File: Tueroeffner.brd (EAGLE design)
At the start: 48.2 x 22.9 mm, 41 parts, among them IC1 NCP1117ST33T3G, IC3 M25PE20, K2 EC2-12TNU, Q1 2N7002CK, Q2 2N7002CK

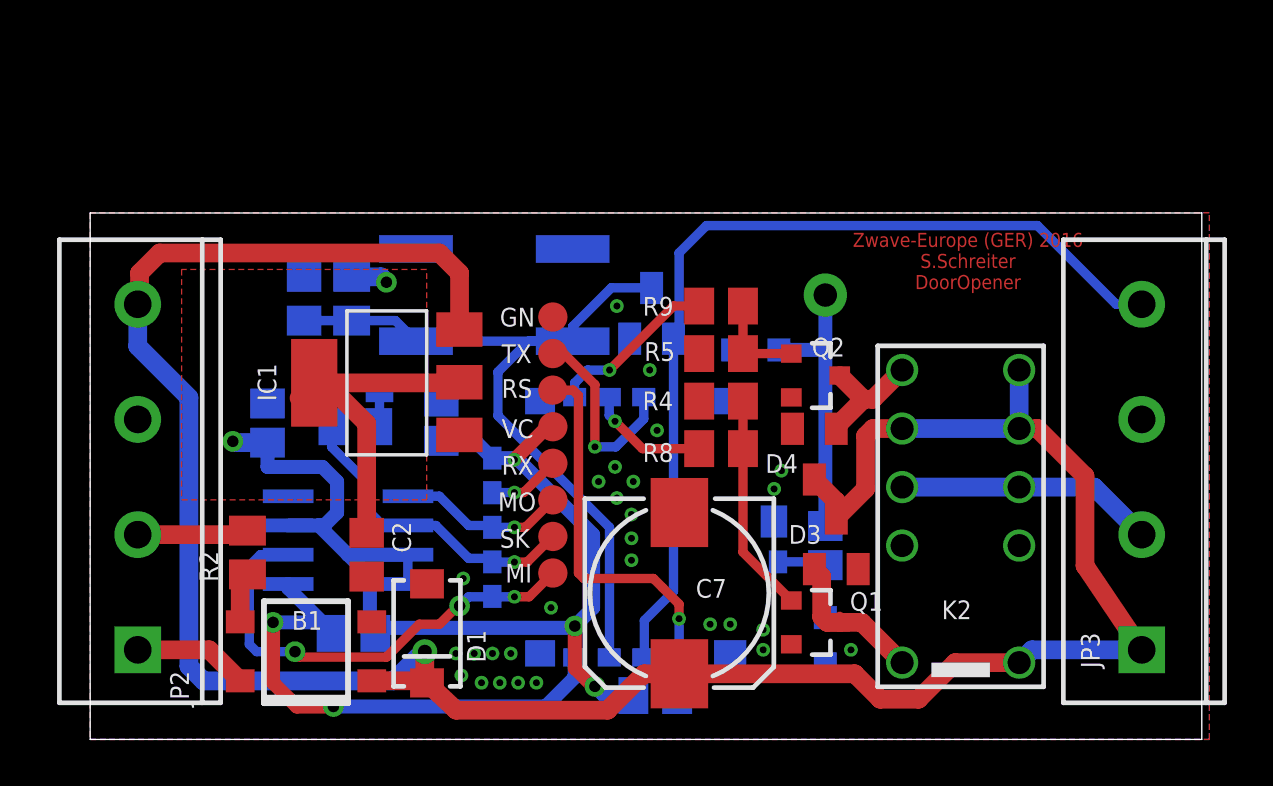
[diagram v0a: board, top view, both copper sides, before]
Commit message: little layout changes
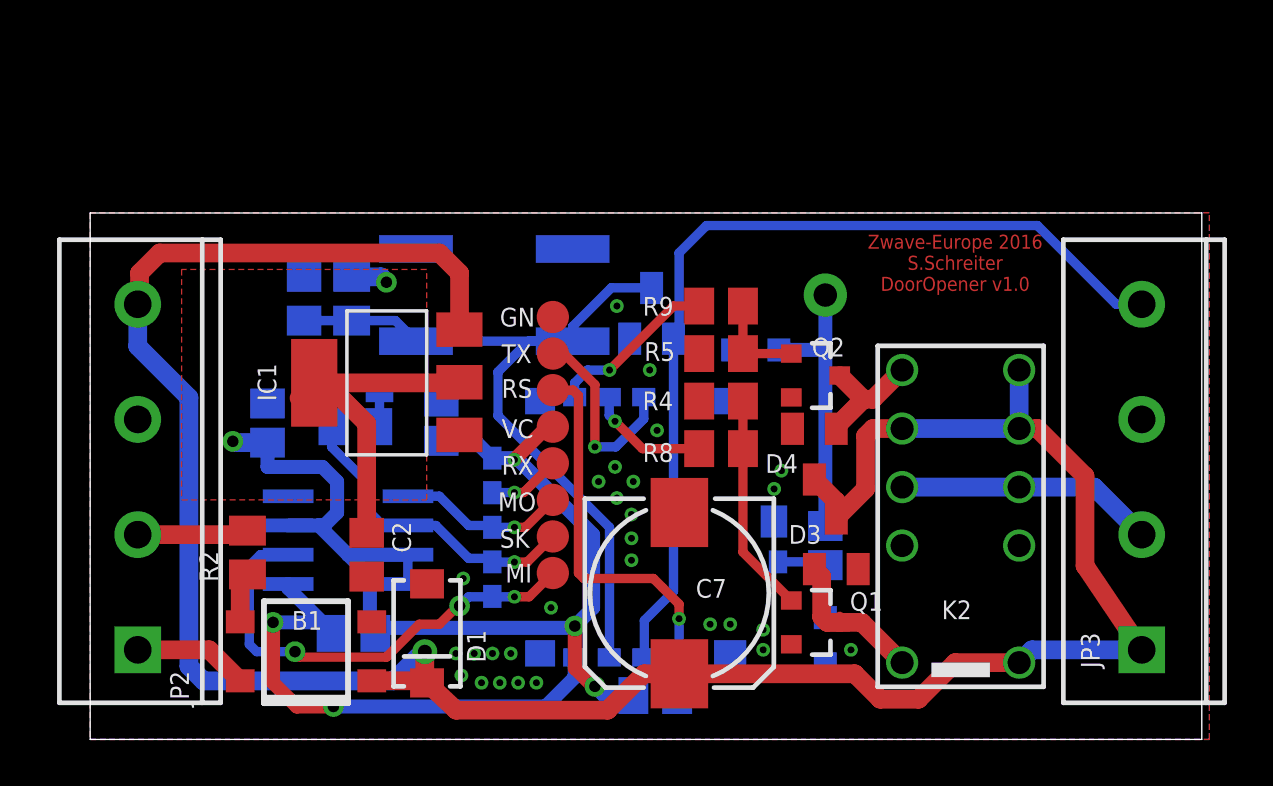
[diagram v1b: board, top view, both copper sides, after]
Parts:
- GN, MI, MO, RS, RX, SK, TX, VC: value TPB1,27 -> TPTP14R; device testpad:B1,27 -> testpad:TP14R
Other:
- board text added: "Zwave-Europe 2016 S.Schreiter DoorOpener v1.0"
- board text removed: "Zwave-Europe (GER) 2016 S.Schreiter DoorOpener"
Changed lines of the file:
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@@
 <layer number="23" name="tOrigins" color="15" fill="1" visible="yes" active="yes"/>
 <layer number="24" name="bOrigins" color="15" fill="1" visible="yes" active="yes"/>
-<layer number="25" name="tNames" color="7" fill="1" visible="yes" active="yes"/>
-<layer number="26" name="bNames" color="7" fill="1" visible="yes" active="yes"/>
+<layer number="25" name="tNames" color="7" fill="1" visible="no" active="yes"/>
+<layer number="26" name="bNames" color="7" fill="1" visible="no" active="yes"/>
 <layer number="27" name="tValues" color="7" fill="1" visible="no" active="yes"/>
 <layer number="28" name="bValues" color="7" fill="1" visible="no" active="yes"/>
@@
 <dimension x1="0" y1="0" x2="0" y2="20" x3="-2" y3="10" textsize="1.778" layer="47"/>
 <dimension x1="0" y1="0" x2="50" y2="0" x3="25" y3="-4" textsize="1.778" layer="47"/>
-<text x="36.5125" y="20.716875" size="0.6096" layer="1" font="vector" ratio="15" rot="R180" align="bottom-center">Zwave-Europe (GER) 2016
+<text x="35.956875" y="20.6375" size="0.6096" layer="1" font="vector" ratio="15" rot="R180" align="bottom-center">Zwave-Europe 2016
 S.Schreiter
-DoorOpener</text>
+DoorOpener v1.0</text>
 <wire x1="46.66" y1="-1.27" x2="46.66" y2="21.59" width="0" layer="20"/>
 </plain>
@@
 <attribute name="VALUE" x="24.526875" y="12.938125" size="1.27" layer="27"/>
 </element>
-<element name="VC" library="testpad" package="B1,27" value="TPB1,27" x="18.494375" y="12.303125" smashed="yes">
+<element name="VC" library="testpad" package="TP14R" value="TPTP14R" x="18.494375" y="12.303125" smashed="yes">
 <attribute name="TP_SIGNAL_NAME" value="" x="17.859375" y="10.398125" size="1" layer="37"/>
 <attribute name="NAME" x="16.271875" y="11.811" size="0.8128" layer="25" ratio="10"/>
 <attribute name="VALUE" x="17.859375" y="11.541125" size="0.0254" layer="27"/>
 </element>
-<element name="RX" library="testpad" package="B1,27" value="TPB1,27" x="18.494375" y="10.715625" smashed="yes">
+<element name="RX" library="testpad" package="TP14R" value="TPTP14R" x="18.494375" y="10.715625" smashed="yes">
 <attribute name="TP_SIGNAL_NAME" value="" x="17.859375" y="8.810625" size="1" layer="37"/>
 <attribute name="NAME" x="16.271875" y="10.2235" size="0.8128" layer="25" ratio="10"/>
 <attribute name="VALUE" x="17.859375" y="9.953625" size="0.0254" layer="27"/>
 </element>
-<element name="TX" library="testpad" package="B1,27" value="TPB1,27" x="18.494375" y="15.478125" smashed="yes">
+<element name="TX" library="testpad" package="TP14R" value="TPTP14R" x="18.494375" y="15.478125" smashed="yes">
 <attribute name="TP_SIGNAL_NAME" value="" x="17.859375" y="13.573125" size="1" layer="37"/>
 <attribute name="NAME" x="16.271875" y="15.065375" size="0.8128" layer="25" ratio="10"/>
 <attribute name="VALUE" x="17.859375" y="14.716125" size="0.0254" layer="27"/>
 </element>
-<element name="GN" library="testpad" package="B1,27" value="TPB1,27" x="18.494375" y="17.065625" smashed="yes">
+<element name="GN" library="testpad" package="TP14R" value="TPTP14R" x="18.494375" y="17.065625" smashed="yes">
 <attribute name="TP_SIGNAL_NAME" value="" x="17.859375" y="15.160625" size="1" layer="37"/>
 <attribute name="NAME" x="16.1925" y="16.652875" size="0.8128" layer="25" ratio="10"/>
 <attribute name="VALUE" x="17.859375" y="16.303625" size="0.0254" layer="27"/>
 </element>
-<element name="MO" library="testpad" package="B1,27" value="TPB1,27" x="18.494375" y="9.128125" smashed="yes">
+<element name="MO" library="testpad" package="TP14R" value="TPTP14R" x="18.494375" y="9.128125" smashed="yes">
 <attribute name="TP_SIGNAL_NAME" value="" x="17.859375" y="7.223125" size="1" layer="37"/>
 <attribute name="NAME" x="16.113125" y="8.636" size="0.8128" layer="25" ratio="10"/>
 <attribute name="VALUE" x="17.859375" y="8.366125" size="0.0254" layer="27"/>
 </element>
-<element name="MI" library="testpad" package="B1,27" value="TPB1,27" x="18.494375" y="5.953125" smashed="yes">
+<element name="MI" library="testpad" package="TP14R" value="TPTP14R" x="18.494375" y="5.953125" smashed="yes">
 <attribute name="TP_SIGNAL_NAME" value="" x="17.859375" y="4.048125" size="1" layer="37"/>
 <attribute name="NAME" x="16.430625" y="5.540375" size="0.8128" layer="25" ratio="10"/>
 <attribute name="VALUE" x="17.859375" y="5.191125" size="0.0254" layer="27"/>
 </element>
-<element name="RS" library="testpad" package="B1,27" value="TPB1,27" x="18.494375" y="13.890625" smashed="yes">
+<element name="RS" library="testpad" package="TP14R" value="TPTP14R" x="18.494375" y="13.890625" smashed="yes">
 <attribute name="TP_SIGNAL_NAME" value="" x="17.859375" y="11.985625" size="1" layer="37"/>
 <attribute name="NAME" x="16.271875" y="13.55725" size="0.8128" layer="25" ratio="10"/>
 <attribute name="VALUE" x="17.859375" y="13.128625" size="0.0254" layer="27"/>
 </element>
-<element name="SK" library="testpad" package="B1,27" value="TPB1,27" x="18.494375" y="7.540625" smashed="yes">
+<element name="SK" library="testpad" package="TP14R" value="TPTP14R" x="18.494375" y="7.540625" smashed="yes">
 <attribute name="TP_SIGNAL_NAME" value="" x="17.859375" y="5.635625" size="1" layer="37"/>
 <attribute name="NAME" x="16.1925" y="7.0485" size="0.8128" layer="25" ratio="10"/>

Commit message: Final RC
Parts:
- added C1: 10µF, eagle-ltspice:C2012
- C6: value 10µF -> 100nF
- IC1: value NCP1117ST33T3G -> NCV4264-2ST33T3G
- LED4: value (none) -> RED
- moved LED4 6.15 mm to (5.16, 17.9), turned to 0 degrees
- moved C2 4.59 mm to (14.4, 9.05)
- moved IC1 1.91 mm to (11.4, 16.1), turned to 270 degrees
- moved C6 1.19 mm to (7.30, 12.5)
- moved R32 0.60 mm to (9.37, 12.5), turned to 90 degrees
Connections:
- net DC_5-12V: now also IC1.1; no longer IC1.3
- net GND: now also C1.2, IC1.2, IC1.4; no longer IC1.1
- net VCC-3.3V: now also C1.1, IC1.3; no longer IC1.2, IC1.4
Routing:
- net DC_5-12V: track 111.0 -> 100.9 mm
- net N$28: track 1.71 -> 5.76 mm
- net VCC-3.3V: track 64.5 -> 66.9 mm
- net BUTTON: track 35.0 -> 33.1 mm
- net RESET: track 17.8 -> 16.1 mm
- net SCK: track 13.7 -> 12.8 mm
- net INT1: track 40.2 -> 39.5 mm
- removed copper zone on layer 1, net VCC-3.3V

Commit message: Add voltage divider
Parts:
- added R6: 180k, resistor:M2012
- added R7: 20k, resistor:M2012
- added SJ1: SOLDERJUMPERTRACE, SparkFun:SJ_2S-TRACE
- moved C2 4.21 mm to (10.8, 11.3), turned to 180 degrees
- moved D1 0.24 mm to (13.0, 3.10)
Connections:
- new net N$2: R6.2, R7.1, SJ1.1
- net DC_5-12V: now also R6.1
- net GND: now also R7.2
- net RXD: now also SJ1.2
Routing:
- net DC_5-12V: track 100.9 -> 113.5 mm
- net N$2: track 0.00 -> 4.73 mm
- net RXD: track 3.16 -> 6.84 mm
- net VCC-3.3V: track 66.9 -> 64.1 mm
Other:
- board text added: "Zwave-Europe 2016 S.Schreiter DoorOpener v1.1"
- board text removed: "Zwave-Europe 2016 S.Schreiter DoorOpener v1.0"

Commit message: BOM
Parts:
- C1, C3: value 10µF -> 100nF
- C5: value 0.1µF -> 100nF
- D1: value SMAJ20A -> SMAJ24A
- IC1: value NCV4264-2ST33T3G -> IFX25001MEV33HTSA1
- R32: value 82 -> 330
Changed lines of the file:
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@@
 <attribute name="VALUE" x="12.064375" y="13.795625" size="1.27" layer="27" rot="R180"/>
 </element>
-<element name="C3" library="eagle-ltspice" package="C2012" value="10µF" x="13.6525" y="12.54125" smashed="yes" rot="MR90">
+<element name="C3" library="eagle-ltspice" package="C2012" value="100nF" x="13.6525" y="12.54125" smashed="yes" rot="MR90">
 <attribute name="SPICEMODEL" value="NONE" x="13.6525" y="12.54125" size="1.778" layer="28" rot="MR90" display="off"/>
 <attribute name="SPICEPREFIX" value="C" x="13.6525" y="12.54125" size="1.778" layer="28" rot="MR90" display="off"/>
@@
 <attribute name="VALUE" x="32.86125" y="8.41375" size="1.27" layer="28" rot="MR270"/>
 </element>
-<element name="C5" library="rcl" package="C0805" value="0.1µF" x="7.699375" y="17.859375" smashed="yes" rot="MR90">
+<element name="C5" library="rcl" package="C0805" value="100nF" x="7.699375" y="17.859375" smashed="yes" rot="MR90">
 <attribute name="NAME" x="8.255" y="20.16125" size="0.8128" layer="26" rot="MR0"/>
 <attribute name="VALUE" x="5.159375" y="16.589375" size="1.27" layer="28" rot="MR90"/>
@@
 <attribute name="VALUE" x="9.8425" y="13.81125" size="1.27" layer="28" rot="MR270"/>
 </element>
-<element name="D1" library="SparkFun-DiscreteSemi" package="SMA-DIODE" value="SMAJ20A" x="13.033125" y="3.09625" smashed="yes" rot="R270">
+<element name="D1" library="SparkFun-DiscreteSemi" package="SMA-DIODE" value="SMAJ24A" x="13.033125" y="3.09625" smashed="yes" rot="R270">
 <attribute name="NAME" x="14.7635" y="3.239125" size="0.8128" layer="25" rot="R270"/>
 <attribute name="VALUE" x="14.684125" y="2.84225" size="0.4064" layer="27" rot="R270"/>
@@
 <attribute name="VALUE" x="24.685625" y="14.049375" size="1.27" layer="28" rot="MR0"/>
 </element>
-<element name="IC1" library="burr-brown" package="SOT223" value="NCV4264-2ST33T3G" x="11.414375" y="16.11375" smashed="yes" rot="R270">
+<element name="IC1" library="burr-brown" package="SOT223" value="IFX25001MEV33HTSA1" x="11.414375" y="16.11375" smashed="yes" rot="R270">
 <attribute name="MPN" value="REG1118-2.85/2K5G4" x="11.414375" y="16.11375" size="1.778" layer="27" rot="R270" display="off"/>
 <attribute name="OC_NEWARK" value="14M2185" x="11.414375" y="16.11375" size="1.778" layer="27" rot="R270" display="off"/>
@@
 <attribute name="VALUE" x="8.5725" y="5.87375" size="1.27" layer="28" rot="MR180"/>
 </element>
-<element name="R32" library="resistor" package="M2012" value="82" x="9.36625" y="12.54125" smashed="yes" rot="MR90">
+<element name="R32" library="resistor" package="M2012" value="330" x="9.36625" y="12.54125" smashed="yes" rot="MR90">
 <attribute name="NAME" x="10.239375" y="14.366875" size="0.8128" layer="26" rot="MR0"/>
 <attribute name="VALUE" x="6.82625" y="11.27125" size="1.27" layer="28" rot="MR90"/>
@@
 <attribute name="VALUE" x="17.859375" y="6.778625" size="0.0254" layer="27"/>
 </element>
-<element name="C1" library="eagle-ltspice" package="C2012" value="10µF" x="11.43" y="12.54125" smashed="yes" rot="MR90">
+<element name="C1" library="eagle-ltspice" package="C2012" value="100nF" x="11.43" y="12.54125" smashed="yes" rot="MR90">
 <attribute name="SPICEMODEL" value="NONE" x="11.43" y="12.54125" size="1.778" layer="28" rot="MR90" display="off"/>
 <attribute name="SPICEPREFIX" value="C" x="11.43" y="12.54125" size="1.778" layer="28" rot="MR90" display="off"/>

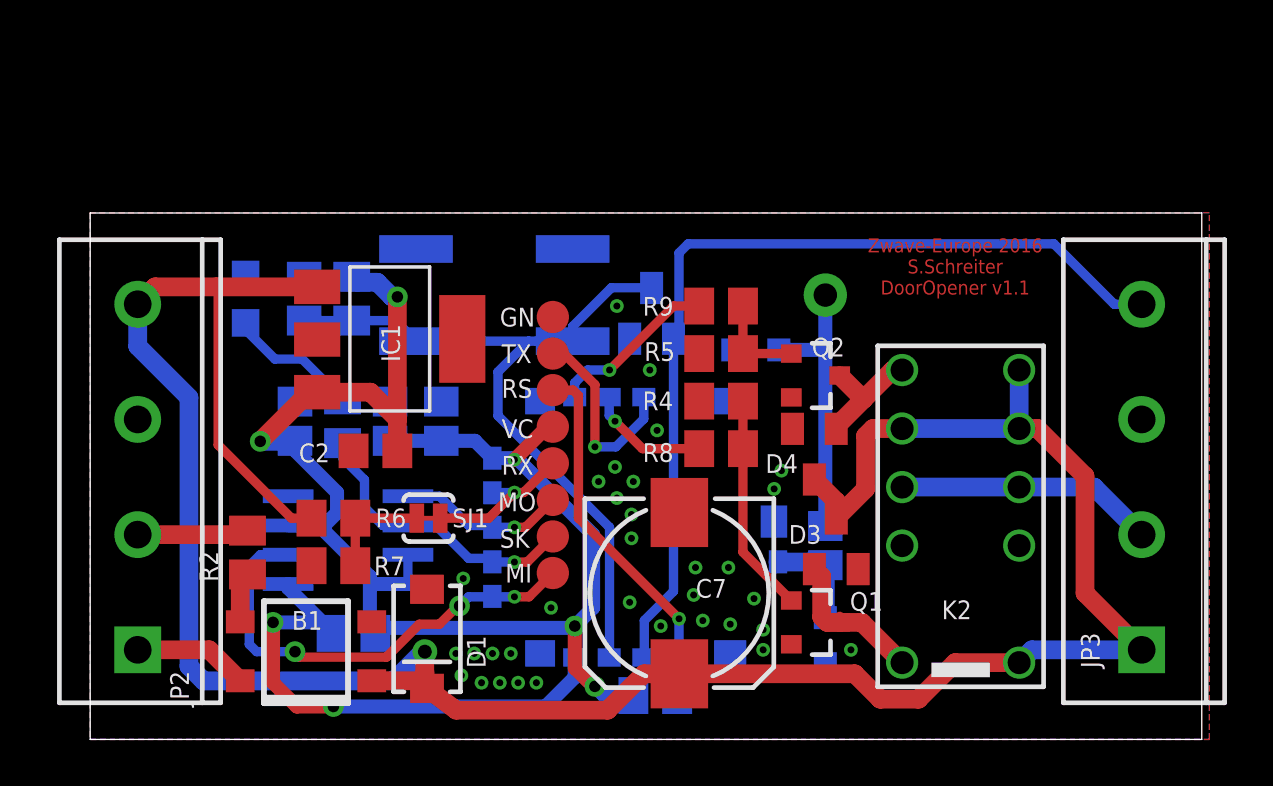
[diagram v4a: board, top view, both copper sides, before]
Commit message: Voltage Divider Cap
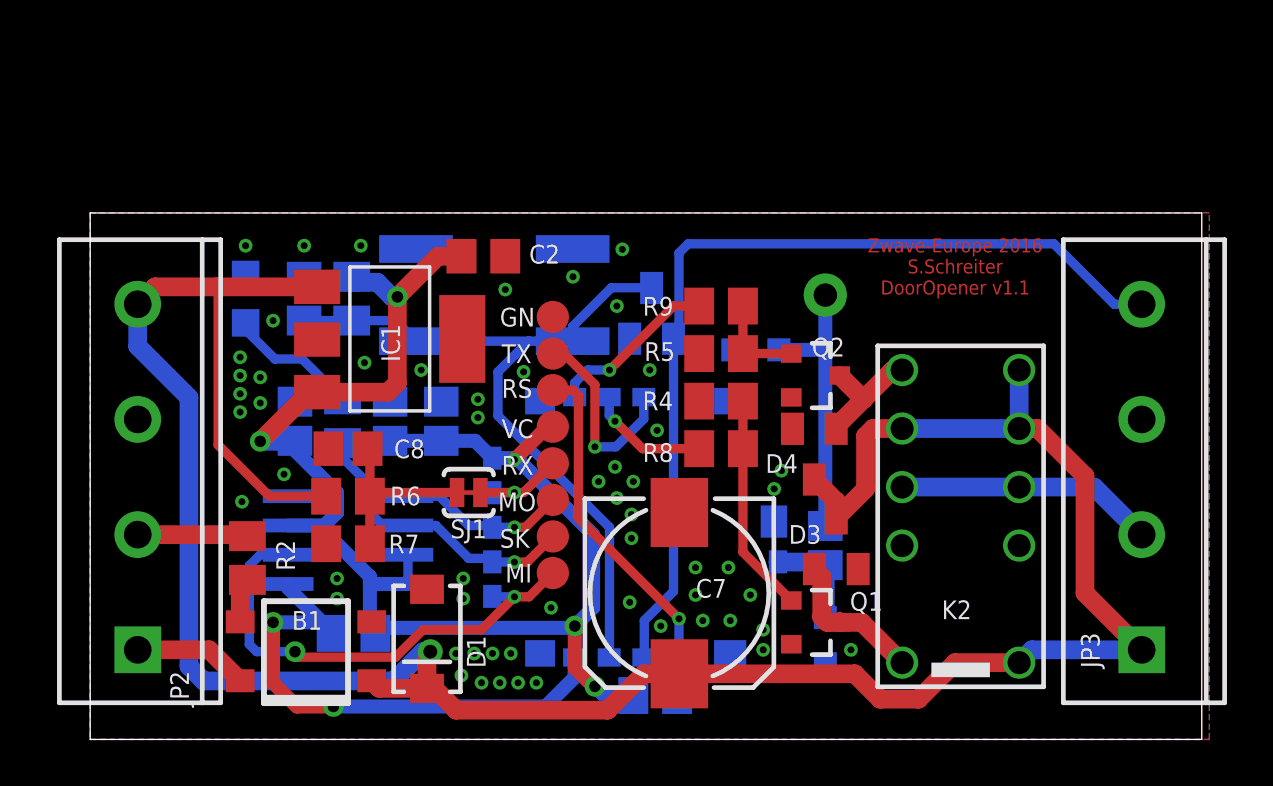
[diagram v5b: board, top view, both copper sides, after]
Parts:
- added C8: 47nF, eagle-ltspice:C2012
- SJ1: value SOLDERJUMPERTRACE -> BATTERY
- moved C2 9.66 mm to (15.5, 19.7), turned to 0 degrees
- moved SJ1 2.07 mm to (14.8, 9.45)
- moved R6 1.14 mm to (9.60, 9.29)
- moved R7 1.14 mm to (9.60, 7.22)
- moved R2 0.24 mm to (5.24, 6.60)
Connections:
- net GND: now also C8.2
- net N$2: now also C8.1
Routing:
- net N$2: track 4.73 -> 8.02 mm
- net RXD: track 6.84 -> 4.63 mm
- net MISO: track 20.3 -> 21.2 mm, vias 3 -> 2
